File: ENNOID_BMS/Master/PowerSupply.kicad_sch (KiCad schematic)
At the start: 33 parts, among them J13 Charger, Q2 BSS138, Q28 BSS138, Q29 BSS138, Q30 BSS138, U19 LM5165YDRC

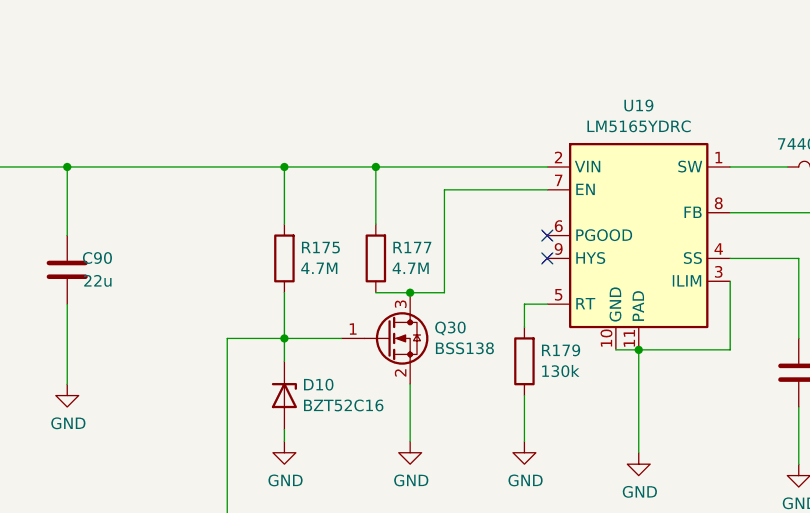
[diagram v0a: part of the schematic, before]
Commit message: updated breakout
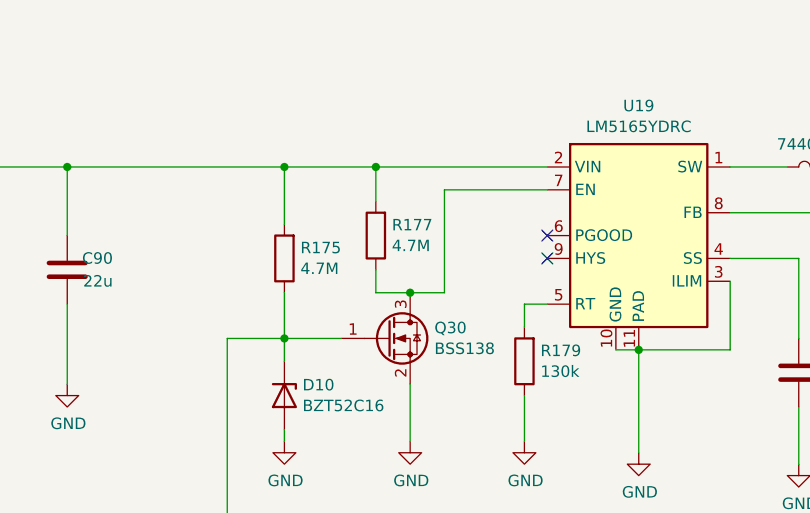
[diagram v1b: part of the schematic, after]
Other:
- moved on the sheet: R177
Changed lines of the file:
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@@
+	(wire
+		(pts
+			(xy 349.25 176.53) (xy 353.06 176.53)
+		)
+		(stroke
+			(width 0)
+			(type default)
+		)
+	)
 	(wire
 		(pts
@@
 	(wire
 		(pts
+			(xy 349.25 166.37) (xy 349.25 162.56)
+		)
+		(stroke
+			(width 0)
+			(type default)
+		)
+	)
+	(wire
+		(pts
 			(xy 370.84 231.14) (xy 363.22 231.14)
 		)
@@
 	(wire
 		(pts
+			(xy 349.25 173.99) (xy 349.25 176.53)
+		)
+		(stroke
+			(width 0)
+			(type default)
+		)
+	)
+	(wire
+		(pts
 			(xy 365.76 187.96) (xy 365.76 193.04)
 		)
@@
 	(wire
 		(pts
-			(xy 349.25 176.53) (xy 353.06 176.53)
-		)
-		(stroke
-			(width 0)
-			(type default)
-		)
-	)
-	(wire
-		(pts
 			(xy 299.72 248.92) (xy 297.18 248.92)
 		)
@@
 		(pts
 			(xy 314.96 177.8) (xy 314.96 186.69)
-		)
-		(stroke
-			(width 0)
-			(type default)
-		)
-	)
-	(wire
-		(pts
-			(xy 349.25 162.56) (xy 349.25 168.91)
 		)
 		(stroke
@@
 	(symbol
 		(lib_id "BMS-Master-rescue:R-Device-BMS-Master-rescue")
-		(at 349.25 172.72 180)
+		(at 349.25 170.18 180)
 		(unit 1)
 		(exclude_from_sim no)
@@
 		(dnp no)
 		(property "Reference" "R177"
-			(at 351.028 171.5516 0)
+			(at 351.028 169.0116 0)
 			(effects
 				(font
@@
 		)
 		(property "Value" "4.7M"
-			(at 351.028 173.863 0)
+			(at 351.028 171.323 0)
 			(effects
 				(font
@@
 		)
 		(property "Footprint" "Resistor_SMD:R_0603_1608Metric"
-			(at 351.028 172.72 90)
+			(at 351.028 170.18 90)
 			(effects
 				(font
@@
 		)
 		(property "Datasheet" "~"
-			(at 349.25 172.72 0)
+			(at 349.25 170.18 0)
 			(effects
 				(font
@@
 		)
 		(property "Description" ""
-			(at 349.25 172.72 0)
+			(at 349.25 170.18 0)
 			(effects
 				(font
@@
 		)
 		(property "MPN" "RC0603FR-074M7L"
-			(at 349.25 172.72 0)
-			(effects
-				(font
+			(at 349.25 170.18 0)
+			(effects
+				(font

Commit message: ENNOID BMS PCBs completed
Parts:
- D10, D11, D12, D13, D7, D8, D9: footprint Diodes_SMD:D_SOD-123 -> Diode_SMD:D_SOD-123
- L3: footprint Inductors_SMD:L_Wuerth_WE-PD2-Typ-MS -> Inductor_SMD:L_Wuerth_WE-PD2-Typ-MS
- Q2, Q28, Q29, Q30: footprint TO_SOT_Packages_SMD:SOT-23 -> Package_TO_SOT_SMD:SOT-23
- U19: footprint Housings_SON:Texas_S-PVSON-N10_ThermalVias -> Package_SON:Texas_S-PVSON-N10_ThermalVias
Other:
- note added: "Diode Or-ing as conditions to turn on the 3.3V regulator power source If any diode is connected to ground, the regulator will enable"
- note added: "PowerButton connects to MCU so most like a reading pin If push button pressed, PowerButton will either go high or low indicating button has been pressed. Need to check firmware, this is unclear"
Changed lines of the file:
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@@
 	(generator_version "9.0")
 	(paper "A2")
+	(text "Diode Or-ing as conditions to turn on the 3.3V regulator power source\nIf any diode is connected to ground, the regulator will enable"
+		(exclude_from_sim no)
+		(at 286.766 143.764 0)
+		(effects
+			(font
+				(size 1.27 1.27)
+			)
+		)
+	)
+	(text "PowerButton connects to MCU so most like a reading pin\nIf push button pressed, \nPowerButton will either go high or low indicating button has been pressed.\nNeed to check firmware, this is unclear"
+		(exclude_from_sim no)
+		(at 228.092 292.354 0)
+		(effects
+			(font
+				(size 1.27 1.27)
+			)
+		)
+	)
 	(junction
 		(at 276.86 248.92)
@@
 			)
 		)
-		(property "Footprint" "Diodes_SMD:D_SOD-123"
+		(property "Footprint" "Diode_SMD:D_SOD-123"
 			(at 344.17 211.455 0)
 			(effects
@@
 			)
 		)
-		(property "Footprint" "Diodes_SMD:D_SOD-123"
+		(property "Footprint" "Diode_SMD:D_SOD-123"
 			(at 345.44 226.695 0)
 			(effects
@@
 			)
 		)
-		(property "Footprint" "Diodes_SMD:D_SOD-123"
+		(property "Footprint" "Diode_SMD:D_SOD-123"
 			(at 345.44 244.475 0)
 			(effects
@@
 			)
 		)
-		(property "Footprint" "Diodes_SMD:D_SOD-123"
+		(property "Footprint" "Diode_SMD:D_SOD-123"
 			(at 316.23 253.365 0)
 			(effects
@@
 			)
 		)
-		(property "Footprint" "Diodes_SMD:D_SOD-123"
+		(property "Footprint" "Diode_SMD:D_SOD-123"
 			(at 285.75 236.855 0)
 			(effects
@@
 			)
 		)
-		(property "Footprint" "Diodes_SMD:D_SOD-123"
+		(property "Footprint" "Diode_SMD:D_SOD-123"
 			(at 272.415 267.97 0)
 			(effects
@@
 			)
 		)
-		(property "Footprint" "Diodes_SMD:D_SOD-123"
+		(property "Footprint" "Diode_SMD:D_SOD-123"
 			(at 334.645 187.96 0)
 			(effects
@@
 			)
 		)
-		(property "Footprint" "Housings_SON:Texas_S-PVSON-N10_ThermalVias"
+		(property "Footprint" "Package_SON:Texas_S-PVSON-N10_ThermalVias"
 			(at 379.73 181.61 0)
 			(effects
@@
 			)
 		)
-		(property "Footprint" "TO_SOT_Packages_SMD:SOT-23"
+		(property "Footprint" "Package_TO_SOT_SMD:SOT-23"
 			(at 355.6 183.515 0)
 			(effects
@@
 			)
 		)
-		(property "Footprint" "Inductors_SMD:L_Wuerth_WE-PD2-Typ-MS"
+		(property "Footprint" "Inductor_SMD:L_Wuerth_WE-PD2-Typ-MS"
 			(at 398.78 162.56 0)
 			(effects
@@
 			)
 		)
-		(property "Footprint" "TO_SOT_Packages_SMD:SOT-23"
+		(property "Footprint" "Package_TO_SOT_SMD:SOT-23"
 			(at 330.2 273.685 0)
 			(effects
@@
 			)
 		)
-		(property "Footprint" "TO_SOT_Packages_SMD:SOT-23"
+		(property "Footprint" "Package_TO_SOT_SMD:SOT-23"
 			(at 242.57 266.065 0)
 			(effects
@@
 			)
 		)
-		(property "Footprint" "TO_SOT_Packages_SMD:SOT-23"
+		(property "Footprint" "Package_TO_SOT_SMD:SOT-23"
 			(at 248.92 210.185 0)
 			(effects

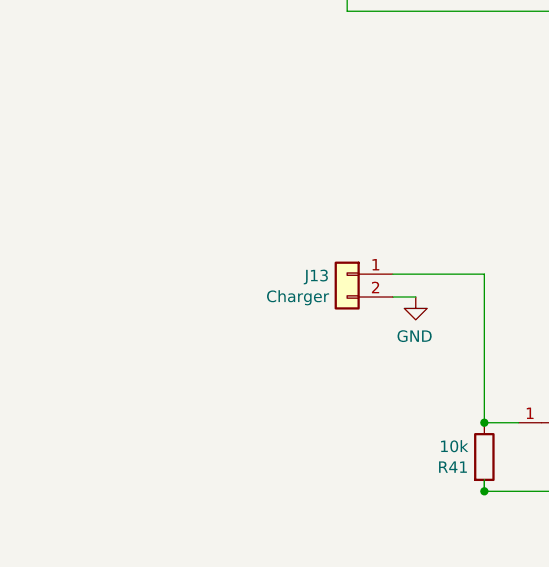
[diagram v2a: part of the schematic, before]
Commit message: bms architecture notes made re charging and discharging
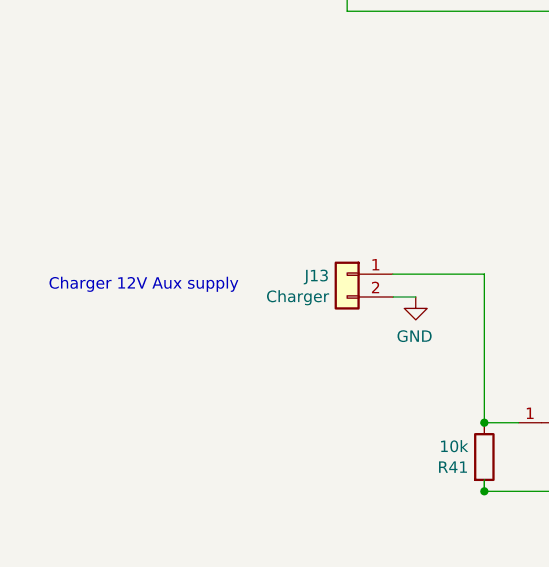
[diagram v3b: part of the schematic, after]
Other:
- note added: "Charger 12V Aux supply"
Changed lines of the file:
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@@
+		)
+	)
+	(text "Charger 12V Aux supply"
+		(exclude_from_sim no)
+		(at 197.104 193.04 0)
+		(effects
+			(font
+				(size 1.27 1.27)
+			)
 		)
 	)

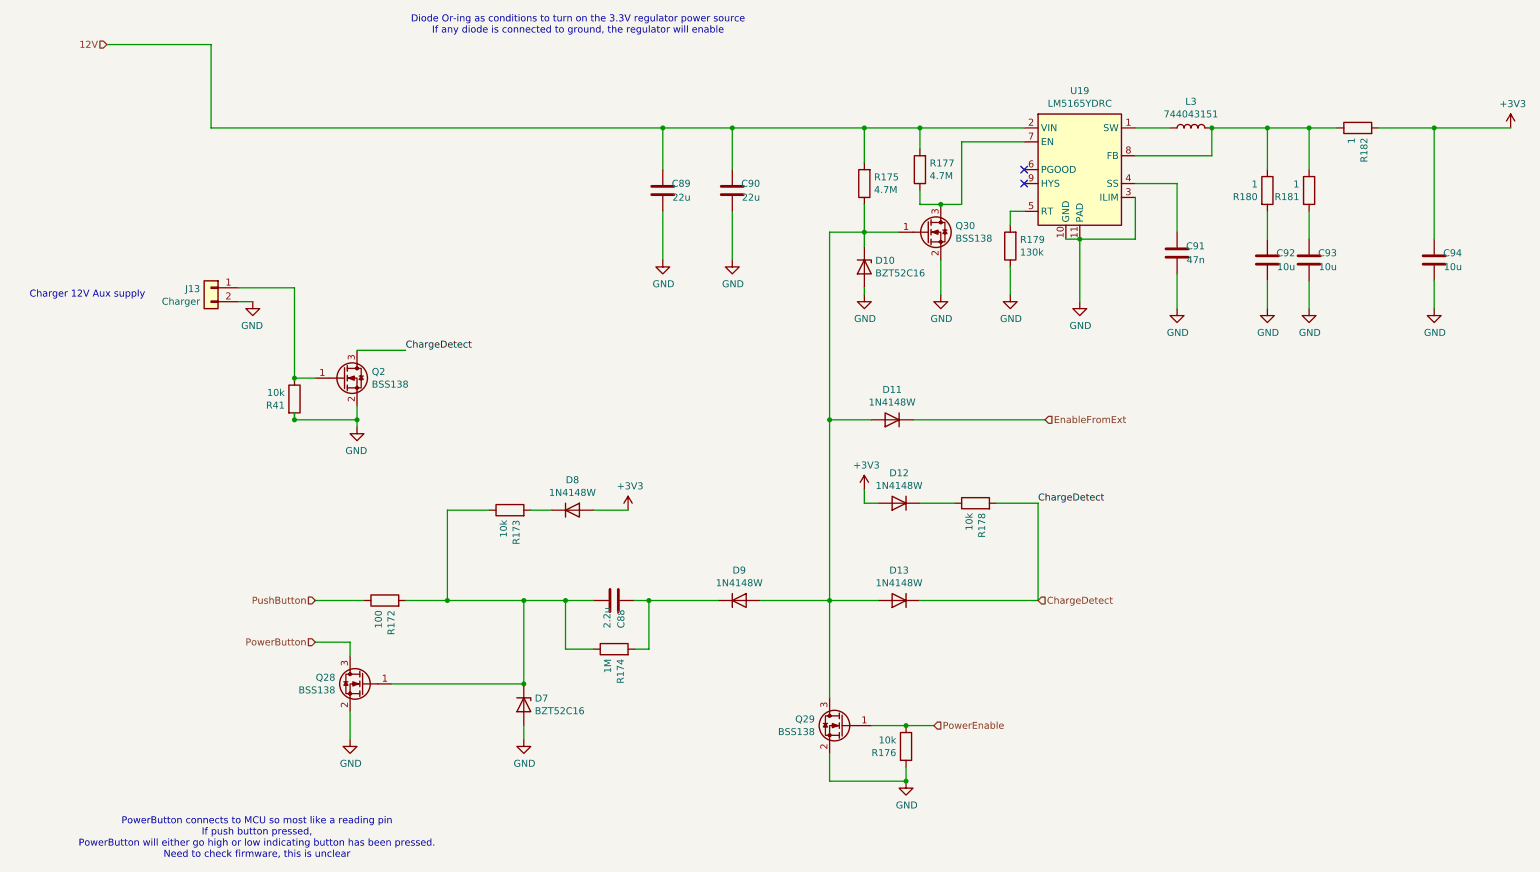
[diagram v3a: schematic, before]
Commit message: Slave with SMD and no other fuses
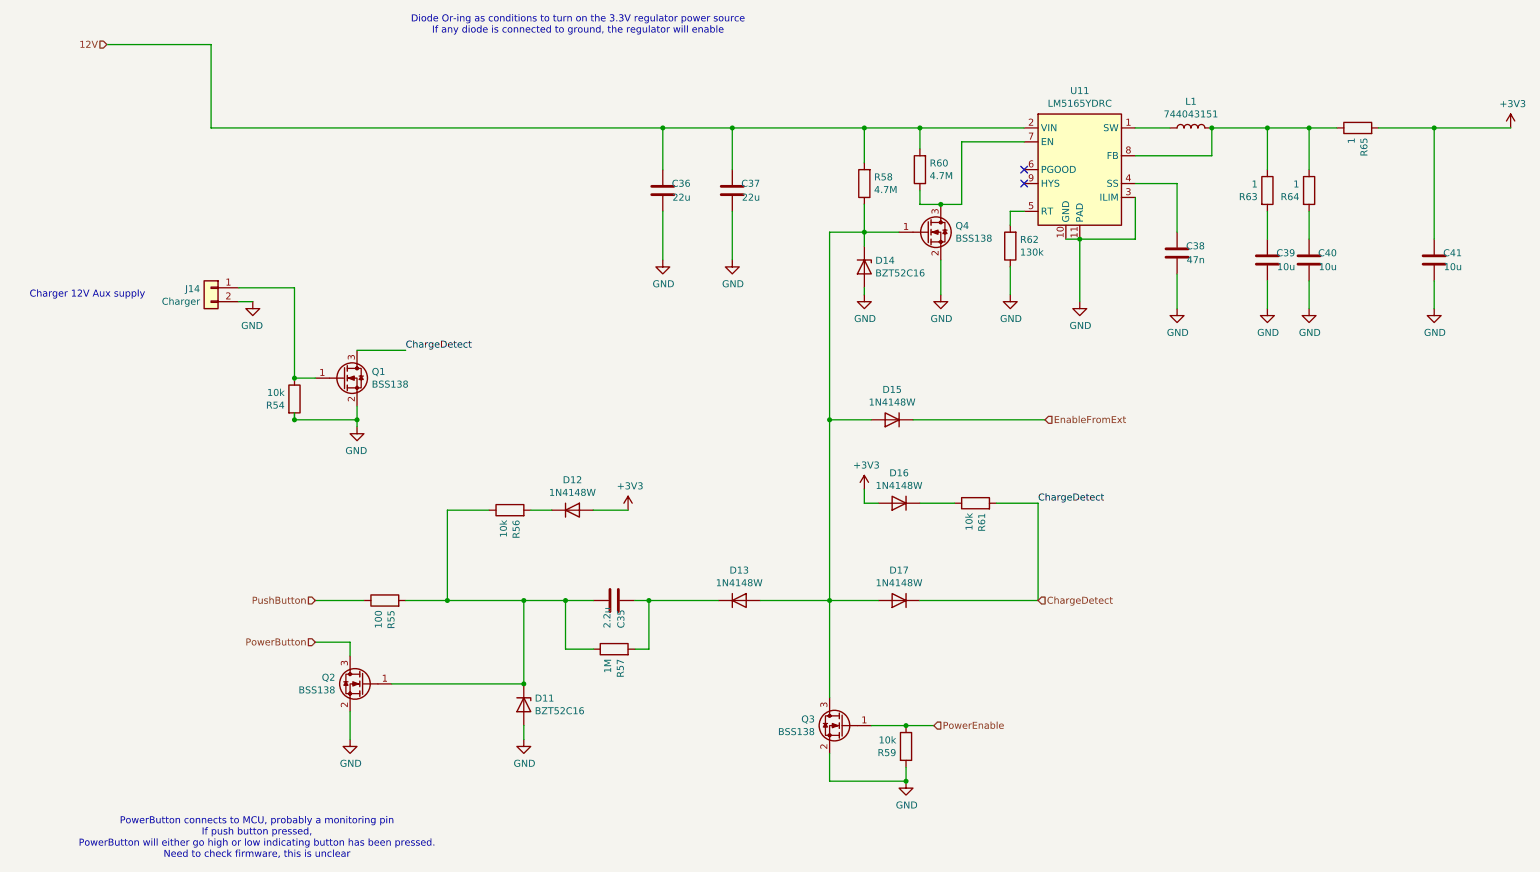
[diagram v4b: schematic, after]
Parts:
- J14: renamed from J13; footprint ENNOID:Pin_1x02-XL -> Connector_JST:JST_XH_B2B-XH-A_1x02_P2.50mm_Vertical; MPN 282834-2 -> B2B-XH-A
- renumbered C88 to C35, C89 to C36, C90 to C37, C91 to C38, C92 to C39, C93 to C40, C94 to C41, D7 to D11, D8 to D12, D9 to D13, D10 to D14, D11 to D15, D12 to D16, D13 to D17, L3 to L1, Q2 to Q1, Q28 to Q2, Q29 to Q3, Q30 to Q4, R41 to R54, R172 to R55, R173 to R56, R174 to R57, R175 to R58, R176 to R59, R177 to R60, R178 to R61, R179 to R62, R180 to R63, R181 to R64, R182 to R65, U19 to U11
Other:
- note added: "PowerButton connects to MCU, probably a monitoring pin If push button pressed, PowerButton will either go high or low indicating button has been pressed. Need to check firmware, this is unclear"
- note removed: "PowerButton connects to MCU so most like a reading pin If push button pressed, PowerButton will either go high or low indicating button has been pressed. Need to check firmware, this is unclear"
